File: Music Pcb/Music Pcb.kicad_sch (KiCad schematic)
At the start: 0 parts

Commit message: worked on skematic added main commponents
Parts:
- added A1: Arduino_Nano_ESP32, Module:Arduino_Nano, symbol MCU_Module:Arduino_Nano_ESP32
- added J1: Conn_01x08, symbol Connector_Generic:Conn_01x08
- added SW1, SW3, SW4: SW_Push, symbol Switch:SW_Push
- added SW2: RotaryEncoder_Switch, symbol Device:RotaryEncoder_Switch
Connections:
- new net: A1.10 (D7), SW2.S1
- new net: A1.5 (D2), SW4.2
- new net: A1.6 (D3), SW3.2
- new net: A1.7 (D4), SW1.2
- new net: A1.8 (D5), SW2.B
- new net: A1.9 (D6), SW2.A
- new net BL: A1.16 (D13/SCK), J1.8 (Pin_8)
- new net CLK: A1.11 (D8), J1.4 (Pin_4)
- new net CS: A1.13 (D10/CS), J1.5 (Pin_5)
- new net DC: A1.14 (D11/COPI), J1.6 (Pin_6)
- new net DIN: A1.12 (D9), J1.3 (Pin_3)
- new net RST: A1.15 (D12/CIPO), J1.7 (Pin_7)
- new net gnd: A1.29 (GND), A1.4 (GND), J1.2 (Pin_2), SW1.1, SW2.C, SW2.S2, SW3.1, SW4.1
- new net vcc: A1.17 (3V3), J1.1 (Pin_1)

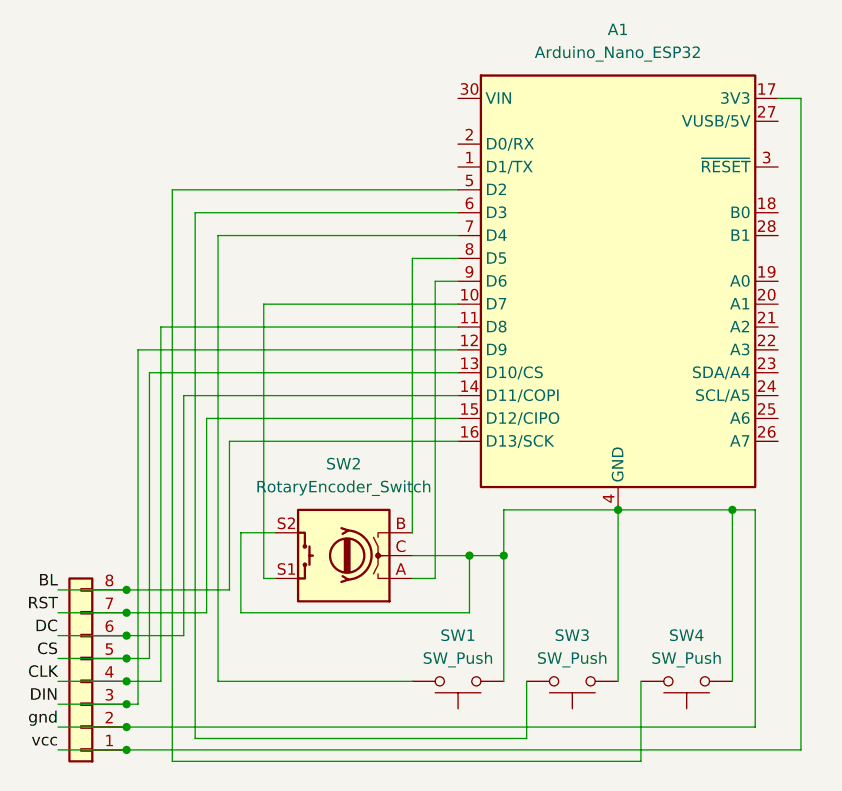
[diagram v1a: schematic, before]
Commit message: added pull up resistors worked on wiring
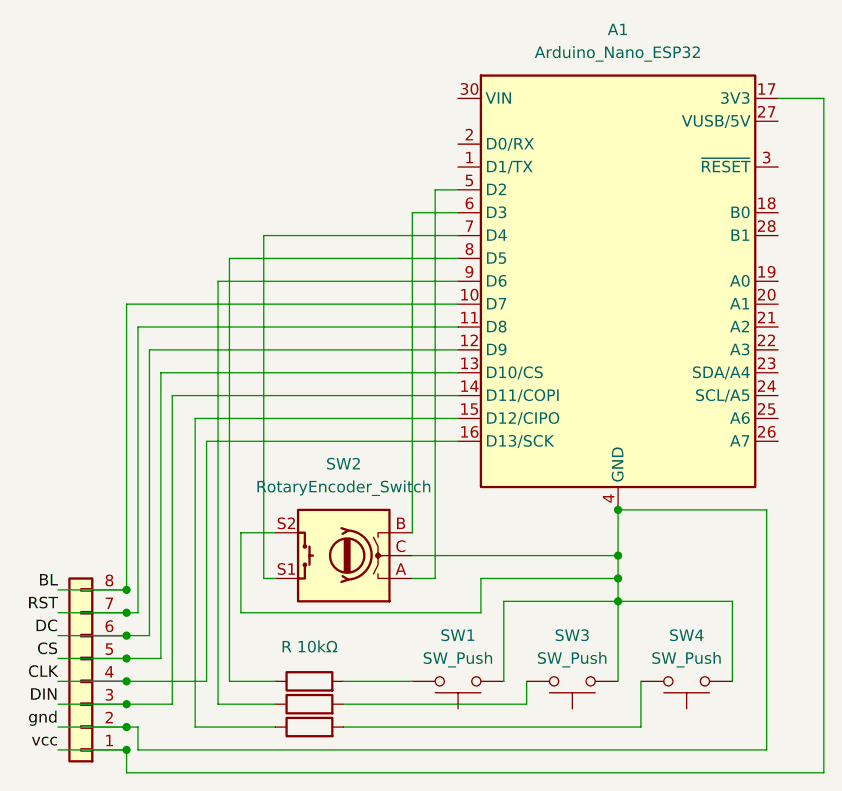
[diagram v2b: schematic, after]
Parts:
- added R1: R 10kΩ, symbol Device:R
- added R2, R3: R, symbol Device:R
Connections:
- net BL: now also A1.10 (D7); no longer A1.16 (D13/SCK)
- net CLK: now also A1.16 (D13/SCK); no longer A1.11 (D8)
- net DC: now also A1.12 (D9); no longer A1.14 (D11/COPI)
- net DIN: now also A1.14 (D11/COPI); no longer A1.12 (D9)
- net RST: now also A1.11 (D8); no longer A1.15 (D12/CIPO)
- net at SW2.S1: now also A1.7 (D4); no longer A1.10 (D7)
- net at A1.5 (D2): now also SW2.A; no longer SW4.2
- net at A1.6 (D3): now also SW2.B; no longer SW3.2
- net at SW1.2: now also R1.2; no longer A1.7 (D4)
- net at A1.8 (D5): now also R1.1; no longer SW2.B
- net at A1.9 (D6): now also R2.1; no longer SW2.A
- new net: A1.15 (D12/CIPO), R3.1
- new net: R3.2, SW4.2
- new net: R2.2, SW3.2
